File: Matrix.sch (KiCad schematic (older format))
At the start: 31 parts

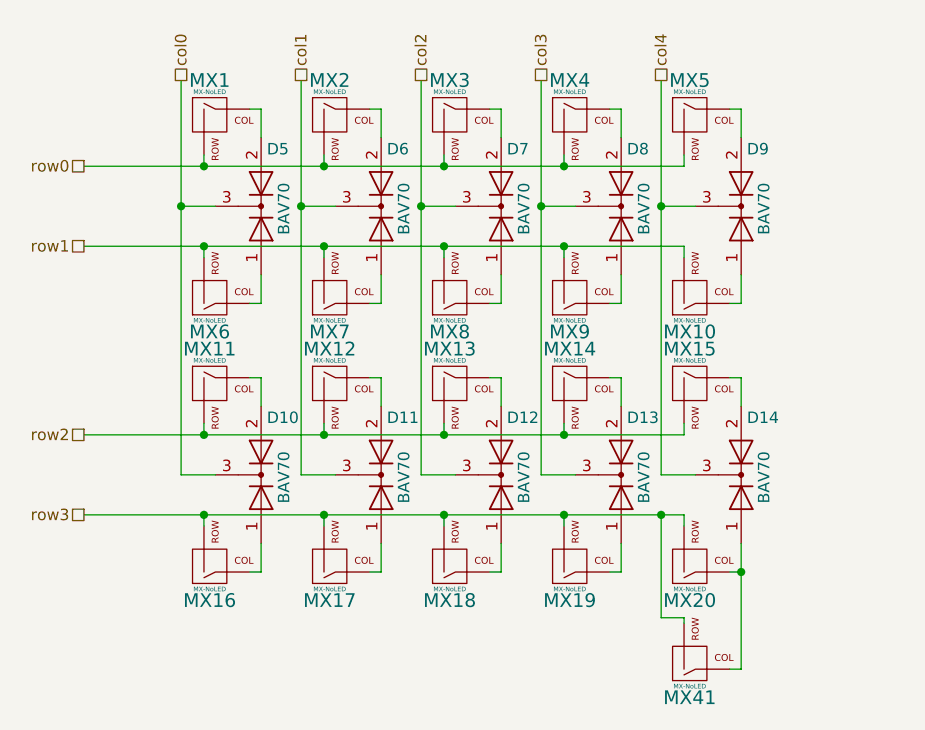
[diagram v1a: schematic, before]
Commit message: Added 3D models, prettied up silk
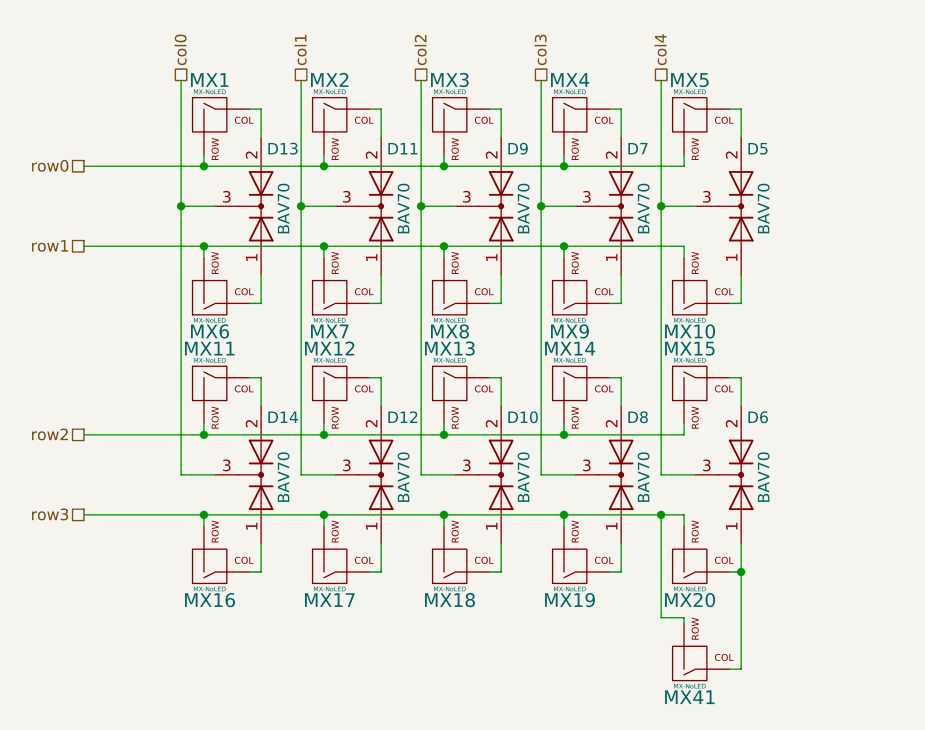
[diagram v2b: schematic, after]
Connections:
- net col0: now also D13.3 (K), D14.3 (K); no longer D10.3 (K), D5.3 (K)
- net col1: now also D12.3 (K); no longer D6.3 (K)
- net col2: now also D10.3 (K), D9.3 (K); no longer D12.3 (K), D7.3 (K)
- net col3: now also D7.3 (K); no longer D13.3 (K)
- net col4: now also D5.3 (K), D6.3 (K); no longer D14.3 (K), D9.3 (K)
- net at MX1.1 (COL): now also D13.2 (A); no longer D5.2 (A)
- net at D5.1 (A): now also MX10.1 (COL); no longer MX6.1 (COL)
- net at MX11.1 (COL): now also D14.2 (A); no longer D10.2 (A)
- net at D10.1 (A): now also MX18.1 (COL); no longer MX16.1 (COL)
- net at MX2.1 (COL): now also D11.2 (A); no longer D6.2 (A)
- net at D6.1 (A): now also MX20.1 (COL), MX41.1 (COL); no longer MX7.1 (COL)
- net at MX12.1 (COL): now also D12.2 (A); no longer D11.2 (A)
- net at D11.1 (A): now also MX7.1 (COL); no longer MX17.1 (COL)
- net at MX3.1 (COL): now also D9.2 (A); no longer D7.2 (A)
- net at D7.1 (A): now also MX9.1 (COL); no longer MX8.1 (COL)
- net at MX13.1 (COL): now also D10.2 (A); no longer D12.2 (A)
- net at D12.1 (A): now also MX17.1 (COL); no longer MX18.1 (COL)
- net at MX4.1 (COL): now also D7.2 (A); no longer D8.2 (A)
- net at D8.1 (A): now also MX19.1 (COL); no longer MX9.1 (COL)
- net at MX14.1 (COL): now also D8.2 (A); no longer D13.2 (A)
- net at D13.1 (A): now also MX6.1 (COL); no longer MX19.1 (COL)
- net at MX5.1 (COL): now also D5.2 (A); no longer D9.2 (A)
- net at D9.1 (A): now also MX8.1 (COL); no longer MX10.1 (COL)
- net at MX15.1 (COL): now also D6.2 (A); no longer D14.2 (A)
- new net: D14.1 (A), MX16.1 (COL)
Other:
- moved on the sheet: D10, D11, D12, D13, D14, D5, D6, D7, D8, D9
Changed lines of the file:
@@
 EESchema Schematic File Version 4
-LIBS:MMboard1-cache
-EELAYER 30 0
+LIBS:mystic_split40-cache
+EELAYER 29 0
 EELAYER END
 $Descr A4 11693 8268
@@
 	1    0    0    -1
 $EndComp
-$Comp
-L Device:D_x2_KCom_AAK D?
-U 1 1 5DC40EEA
-P 4950 3175
-AR Path="/5DC40EEA" Ref="D?"  Part="1"
-AR Path="/5DBF64D6/5DC40EEA" Ref="D5"  Part="1"
-AR Path="/5E0FF211/5DC40EEA" Ref="D?"  Part="1"
-AR Path="/5E103021/5DC40EEA" Ref="D15"  Part="1"
-F 0 "D5" V 5200 3200 50  0000 L CNN
-F 1 "BAV70" H 4825 3275 50  0000 L CNN
-F 2 "Package_TO_SOT_SMD:SOT-23_Handsoldering" H 4950 3175 50  0001 C CNN
-F 3 "~" H 4950 3175 50  0001 C CNN
-	1    4950 3175
-	0    1    -1   0
-$EndComp
 Wire Wire Line
 	4900 3600 4950 3600
@@
 L Device:D_x2_KCom_AAK D?
 U 1 1 5DC4E722
-P 4950 4350
+P 6000 4350
 AR Path="/5DC4E722" Ref="D?"  Part="1"
 AR Path="/5DBF64D6/5DC4E722" Ref="D10"  Part="1"
 AR Path="/5E0FF211/5DC4E722" Ref="D?"  Part="1"
 AR Path="/5E103021/5DC4E722" Ref="D20"  Part="1"
-F 0 "D10" V 5200 4375 50  0000 L CNN
-F 1 "BAV70" H 4825 4450 50  0000 L CNN
-F 2 "Package_TO_SOT_SMD:SOT-23_Handsoldering" H 4950 4350 50  0001 C CNN
-F 3 "~" H 4950 4350 50  0001 C CNN
-	1    4950 4350
+F 0 "D10" V 6250 4375 50  0000 L CNN
+F 1 "BAV70" H 5875 4450 50  0000 L CNN
+F 2 "Package_TO_SOT_SMD:SOT-23_Handsoldering" H 6000 4350 50  0001 C CNN
+F 3 "~" H 6000 4350 50  0001 C CNN
+	1    6000 4350
 	0    1    -1   0
 $EndComp
@@
 	1    0    0    -1
 $EndComp
-$Comp
-L Device:D_x2_KCom_AAK D?
-U 1 1 5DC54A9C
-P 5475 3175
-AR Path="/5DC54A9C" Ref="D?"  Part="1"
-AR Path="/5DBF64D6/5DC54A9C" Ref="D6"  Part="1"
-AR Path="/5E0FF211/5DC54A9C" Ref="D?"  Part="1"
-AR Path="/5E103021/5DC54A9C" Ref="D16"  Part="1"
-F 0 "D6" V 5725 3200 50  0000 L CNN
-F 1 "BAV70" H 5350 3275 50  0000 L CNN
-F 2 "Package_TO_SOT_SMD:SOT-23_Handsoldering" H 5475 3175 50  0001 C CNN
-F 3 "~" H 5475 3175 50  0001 C CNN
-	1    5475 3175
-	0    1    -1   0
-$EndComp
 Wire Wire Line
 	5425 3600 5475 3600
@@
 L Device:D_x2_KCom_AAK D?
 U 1 1 5DC54AC1
-P 5475 4350
+P 5475 3175
 AR Path="/5DC54AC1" Ref="D?"  Part="1"
 AR Path="/5DBF64D6/5DC54AC1" Ref="D11"  Part="1"
 AR Path="/5E0FF211/5DC54AC1" Ref="D?"  Part="1"
 AR Path="/5E103021/5DC54AC1" Ref="D21"  Part="1"
-F 0 "D11" V 5725 4375 50  0000 L CNN
-F 1 "BAV70" H 5350 4450 50  0000 L CNN
-F 2 "Package_TO_SOT_SMD:SOT-23_Handsoldering" H 5475 4350 50  0001 C CNN
-F 3 "~" H 5475 4350 50  0001 C CNN
-	1    5475 4350
+F 0 "D11" V 5725 3200 50  0000 L CNN
+F 1 "BAV70" H 5350 3275 50  0000 L CNN
+F 2 "Package_TO_SOT_SMD:SOT-23_Handsoldering" H 5475 3175 50  0001 C CNN
+F 3 "~" H 5475 3175 50  0001 C CNN
+	1    5475 3175
 	0    1    -1   0
 $EndComp
@@
 	1    0    0    -1
 $EndComp
-$Comp
-L Device:D_x2_KCom_AAK D?
-U 1 1 5DC60A34
-P 6000 3175
-AR Path="/5DC60A34" Ref="D?"  Part="1"
-AR Path="/5DBF64D6/5DC60A34" Ref="D7"  Part="1"
-AR Path="/5E0FF211/5DC60A34" Ref="D?"  Part="1"
-AR Path="/5E103021/5DC60A34" Ref="D17"  Part="1"
-F 0 "D7" V 6250 3200 50  0000 L CNN
-F 1 "BAV70" H 5875 3275 50  0000 L CNN
-F 2 "Package_TO_SOT_SMD:SOT-23_Handsoldering" H 6000 3175 50  0001 C CNN
-F 3 "~" H 6000 3175 50  0001 C CNN
-	1    6000 3175
-	0    1    -1   0
-$EndComp
 Wire Wire Line
 	5950 3600 6000 3600
@@
 L Device:D_x2_KCom_AAK D?
 U 1 1 5DC60A59
-P 6000 4350
+P 5475 4350
 AR Path="/5DC60A59" Ref="D?"  Part="1"
 AR Path="/5DBF64D6/5DC60A59" Ref="D12"  Part="1"
 AR Path="/5E0FF211/5DC60A59" Ref="D?"  Part="1"
 AR Path="/5E103021/5DC60A59" Ref="D22"  Part="1"
-F 0 "D12" V 6250 4375 50  0000 L CNN
-F 1 "BAV70" H 5875 4450 50  0000 L CNN
-F 2 "Package_TO_SOT_SMD:SOT-23_Handsoldering" H 6000 4350 50  0001 C CNN
-F 3 "~" H 6000 4350 50  0001 C CNN
-	1    6000 4350
+F 0 "D12" V 5725 4375 50  0000 L CNN
+F 1 "BAV70" H 5350 4450 50  0000 L CNN
+F 2 "Package_TO_SOT_SMD:SOT-23_Handsoldering" H 5475 4350 50  0001 C CNN
+F 3 "~" H 5475 4350 50  0001 C CNN
+	1    5475 4350
 	0    1    -1   0
 $EndComp
@@
 	1    0    0    -1
 $EndComp
-$Comp
-L Device:D_x2_KCom_AAK D?
-U 1 1 5DC60A81
-P 6525 3175
-AR Path="/5DC60A81" Ref="D?"  Part="1"
-AR Path="/5DBF64D6/5DC60A81" Ref="D8"  Part="1"
-AR Path="/5E0FF211/5DC60A81" Ref="D?"  Part="1"
-AR Path="/5E103021/5DC60A81" Ref="D18"  Part="1"
-F 0 "D8" V 6775 3200 50  0000 L CNN
-F 1 "BAV70" H 6400 3275 50  0000 L CNN
-F 2 "Package_TO_SOT_SMD:SOT-23_Handsoldering" H 6525 3175 50  0001 C CNN
-F 3 "~" H 6525 3175 50  0001 C CNN
-	1    6525 3175
-	0    1    -1   0
-$EndComp
 Wire Wire Line
 	6475 3600 6525 3600
@@
 	1    0    0    -1
 $EndComp
-$Comp
-L Device:D_x2_KCom_AAK D?
-U 1 1 5DC60AA6
-P 6525 4350
-AR Path="/5DC60AA6" Ref="D?"  Part="1"
-AR Path="/5DBF64D6/5DC60AA6" Ref="D13"  Part="1"
-AR Path="/5E0FF211/5DC60AA6" Ref="D?"  Part="1"
-AR Path="/5E103021/5DC60AA6" Ref="D23"  Part="1"
-F 0 "D13" V 6775 4375 50  0000 L CNN
-F 1 "BAV70" H 6400 4450 50  0000 L CNN
-F 2 "Package_TO_SOT_SMD:SOT-23_Handsoldering" H 6525 4350 50  0001 C CNN
-F 3 "~" H 6525 4350 50  0001 C CNN
-	1    6525 4350
-	0    1    -1   0
-$EndComp
 Wire Wire Line
 	6475 4775 6525 4775
@@
 	1    0    0    -1
 $EndComp
-$Comp
-L Device:D_x2_KCom_AAK D?
-U 1 1 5DC6C6C7
-P 7050 3175
-AR Path="/5DC6C6C7" Ref="D?"  Part="1"
-AR Path="/5DBF64D6/5DC6C6C7" Ref="D9"  Part="1"
-AR Path="/5E0FF211/5DC6C6C7" Ref="D?"  Part="1"
-AR Path="/5E103021/5DC6C6C7" Ref="D19"  Part="1"
-F 0 "D9" V 7300 3200 50  0000 L CNN
-F 1 "BAV70" H 6925 3275 50  0000 L CNN
-F 2 "Package_TO_SOT_SMD:SOT-23_Handsoldering" H 7050 3175 50  0001 C CNN
-F 3 "~" H 7050 3175 50  0001 C CNN
-	1    7050 3175
-	0    1    -1   0
-$EndComp
 Wire Wire Line
 	7000 3600 7050 3600
@@
 	1    6850 3975
 	1    0    0    -1
-$EndComp
-$Comp
-L Device:D_x2_KCom_AAK D?
-U 1 1 5DC6C6EC
-P 7050 4350
-AR Path="/5DC6C6EC" Ref="D?"  Part="1"
-AR Path="/5DBF64D6/5DC6C6EC" Ref="D14"  Part="1"
-AR Path="/5E0FF211/5DC6C6EC" Ref="D?"  Part="1"
-AR Path="/5E103021/5DC6C6EC" Ref="D24"  Part="1"
-F 0 "D14" V 7300 4375 50  0000 L CNN
-F 1 "BAV70" H 6925 4450 50  0000 L CNN
-F 2 "Package_TO_SOT_SMD:SOT-23_Handsoldering" H 7050 4350 50  0001 C CNN
-F 3 "~" H 7050 4350 50  0001 C CNN
-	1    7050 4350
-	0    1    -1   0
 $EndComp
 Wire Wire Line
@@
 Wire Wire Line
 	6700 4975 6700 4525
+$Comp
+L Device:D_x2_KCom_AAK D?
+U 1 1 5DC60AA6
+P 4950 3175
+AR Path="/5DC60AA6" Ref="D?"  Part="1"
+AR Path="/5DBF64D6/5DC60AA6" Ref="D13"  Part="1"
+AR Path="/5E0FF211/5DC60AA6" Ref="D?"  Part="1"
+AR Path="/5E103021/5DC60AA6" Ref="D23"  Part="1"
+F 0 "D13" V 5200 3200 50  0000 L CNN
+F 1 "BAV70" H 4825 3275 50  0000 L CNN
+F 2 "Package_TO_SOT_SMD:SOT-23_Handsoldering" H 4950 3175 50  0001 C CNN
+F 3 "~" H 4950 3175 50  0001 C CNN
+	1    4950 3175
+	0    1    -1   0
+$EndComp
+$Comp
+L Device:D_x2_KCom_AAK D?
+U 1 1 5DC60A34
+P 6525 3175
+AR Path="/5DC60A34" Ref="D?"  Part="1"
+AR Path="/5DBF64D6/5DC60A34" Ref="D7"  Part="1"
+AR Path="/5E0FF211/5DC60A34" Ref="D?"  Part="1"
+AR Path="/5E103021/5DC60A34" Ref="D17"  Part="1"
+F 0 "D7" V 6775 3200 50  0000 L CNN
+F 1 "BAV70" H 6400 3275 50  0000 L CNN
+F 2 "Package_TO_SOT_SMD:SOT-23_Handsoldering" H 6525 3175 50  0001 C CNN
+F 3 "~" H 6525 3175 50  0001 C CNN
+	1    6525 3175
+	0    1    -1   0
+$EndComp
+$Comp
+L Device:D_x2_KCom_AAK D?
+U 1 1 5DC60A81
+P 6525 4350
+AR Path="/5DC60A81" Ref="D?"  Part="1"
+AR Path="/5DBF64D6/5DC60A81" Ref="D8"  Part="1"
+AR Path="/5E0FF211/5DC60A81" Ref="D?"  Part="1"
+AR Path="/5E103021/5DC60A81" Ref="D18"  Part="1"
+F 0 "D8" V 6775 4375 50  0000 L CNN
+F 1 "BAV70" H 6400 4450 50  0000 L CNN
+F 2 "Package_TO_SOT_SMD:SOT-23_Handsoldering" H 6525 4350 50  0001 C CNN
+F 3 "~" H 6525 4350 50  0001 C CNN
+	1    6525 4350
+	0    1    -1   0
+$EndComp
+$Comp
+L Device:D_x2_KCom_AAK D?
+U 1 1 5DC6C6EC
+P 4950 4350
+AR Path="/5DC6C6EC" Ref="D?"  Part="1"
+AR Path="/5DBF64D6/5DC6C6EC" Ref="D14"  Part="1"
+AR Path="/5E0FF211/5DC6C6EC" Ref="D?"  Part="1"
+AR Path="/5E103021/5DC6C6EC" Ref="D24"  Part="1"
+F 0 "D14" V 5200 4375 50  0000 L CNN
+F 1 "BAV70" H 4825 4450 50  0000 L CNN
+F 2 "Package_TO_SOT_SMD:SOT-23_Handsoldering" H 4950 4350 50  0001 C CNN
+F 3 "~" H 4950 4350 50  0001 C CNN
+	1    4950 4350
+	0    1    -1   0
+$EndComp
+$Comp
+L Device:D_x2_KCom_AAK D?
+U 1 1 5DC54A9C
+P 7050 4350
+AR Path="/5DC54A9C" Ref="D?"  Part="1"
+AR Path="/5DBF64D6/5DC54A9C" Ref="D6"  Part="1"
+AR Path="/5E0FF211/5DC54A9C" Ref="D?"  Part="1"
+AR Path="/5E103021/5DC54A9C" Ref="D16"  Part="1"
+F 0 "D6" V 7300 4375 50  0000 L CNN
+F 1 "BAV70" H 6925 4450 50  0000 L CNN
+F 2 "Package_TO_SOT_SMD:SOT-23_Handsoldering" H 7050 4350 50  0001 C CNN
+F 3 "~" H 7050 4350 50  0001 C CNN
+	1    7050 4350
+	0    1    -1   0
+$EndComp
+$Comp
+L Device:D_x2_KCom_AAK D?
+U 1 1 5DC6C6C7
+P 6000 3175
+AR Path="/5DC6C6C7" Ref="D?"  Part="1"
+AR Path="/5DBF64D6/5DC6C6C7" Ref="D9"  Part="1"
+AR Path="/5E0FF211/5DC6C6C7" Ref="D?"  Part="1"
+AR Path="/5E103021/5DC6C6C7" Ref="D19"  Part="1"
+F 0 "D9" V 6250 3200 50  0000 L CNN
+F 1 "BAV70" H 5875 3275 50  0000 L CNN
+F 2 "Package_TO_SOT_SMD:SOT-23_Handsoldering" H 6000 3175 50  0001 C CNN
+F 3 "~" H 6000 3175 50  0001 C CNN
+	1    6000 3175
+	0    1    -1   0
+$EndComp
+$Comp
+L Device:D_x2_KCom_AAK D?
+U 1 1 5DC40EEA
+P 7050 3175
+AR Path="/5DC40EEA" Ref="D?"  Part="1"
+AR Path="/5DBF64D6/5DC40EEA" Ref="D5"  Part="1"
+AR Path="/5E0FF211/5DC40EEA" Ref="D?"  Part="1"
+AR Path="/5E103021/5DC40EEA" Ref="D15"  Part="1"
+F 0 "D5" V 7300 3200 50  0000 L CNN
+F 1 "BAV70" H 6925 3275 50  0000 L CNN
+F 2 "Package_TO_SOT_SMD:SOT-23_Handsoldering" H 7050 3175 50  0001 C CNN
+F 3 "~" H 7050 3175 50  0001 C CNN
+	1    7050 3175
+	0    1    -1   0
+$EndComp
 $EndSCHEMATC
